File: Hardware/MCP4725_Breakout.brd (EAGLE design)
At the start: 15.2 x 15.2 mm, 17 parts, among them U1 DAC_MCP4725SOT-CP

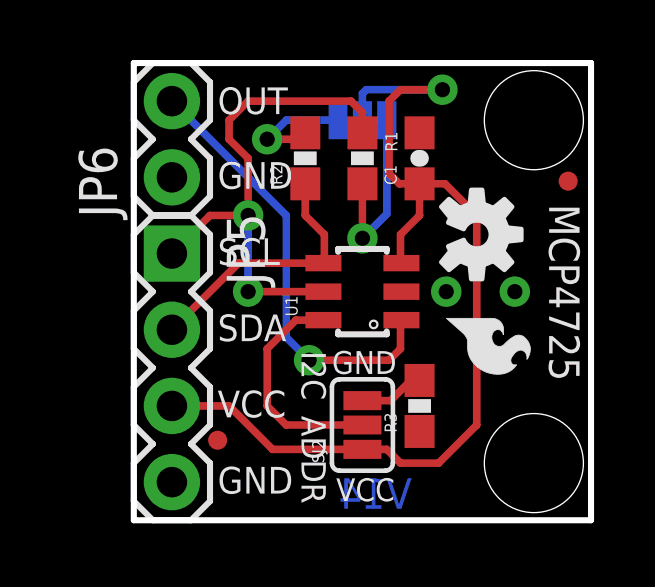
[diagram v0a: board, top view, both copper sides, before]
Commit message: Last Commit before Reds
Added my name to brd. file
added Vcc levels to sch.
changed file name so version # isn't there
minor silk fixes due to vias.
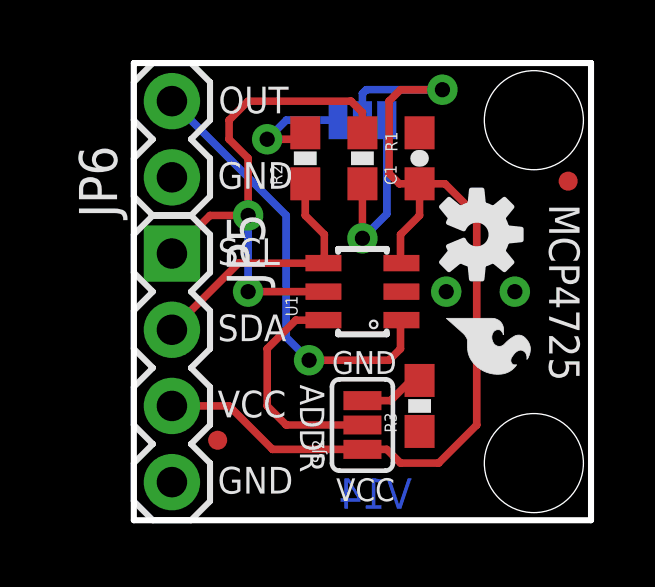
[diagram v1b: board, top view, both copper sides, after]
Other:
- board text added: "Joel Bartlett"
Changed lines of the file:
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@@
 <text x="2.794" y="8.509" size="0.889" layer="21" ratio="15">SCL</text>
 <text x="2.794" y="3.429" size="0.889" layer="21" ratio="15">VCC</text>
-<text x="2.794" y="13.5382" size="0.889" layer="21" ratio="15">OUT</text>
+<text x="2.8194" y="13.5636" size="0.889" layer="21" ratio="15">OUT</text>
 <text x="13.843" y="10.541" size="1.016" layer="21" ratio="15" rot="SR270">MCP4725</text>
 <text x="9.271" y="0.381" size="1.016" layer="16" font="vector" ratio="15" rot="SMR0">V14</text>
-<text x="5.588" y="5.6388" size="0.8128" layer="21" font="vector" ratio="15" rot="SR270">I2C</text>
-<text x="5.588" y="3.4798" size="0.8128" layer="21" font="vector" ratio="15" rot="SR270">ADDR</text>
+<text x="5.5372" y="4.5212" size="0.8128" layer="21" font="vector" ratio="15" rot="SR270">ADDR</text>
 <text x="5.207" y="13.97" size="1.016" layer="22" ratio="15" rot="MR0" align="center-left">OUT</text>
 <text x="5.207" y="8.89" size="1.016" layer="22" ratio="15" rot="MR0" align="center-left">SCL</text>
@@
 <text x="2.794" y="11.049" size="0.889" layer="21" ratio="15">GND</text>
 <text x="5.207" y="11.43" size="1.016" layer="22" ratio="15" rot="MR0" align="center-left">GND</text>
+<text x="52.07" y="-21.59" size="1.778" layer="51">Joel Bartlett</text>
 </plain>
 <attributes>

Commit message: removed micro fiducial, added regulars
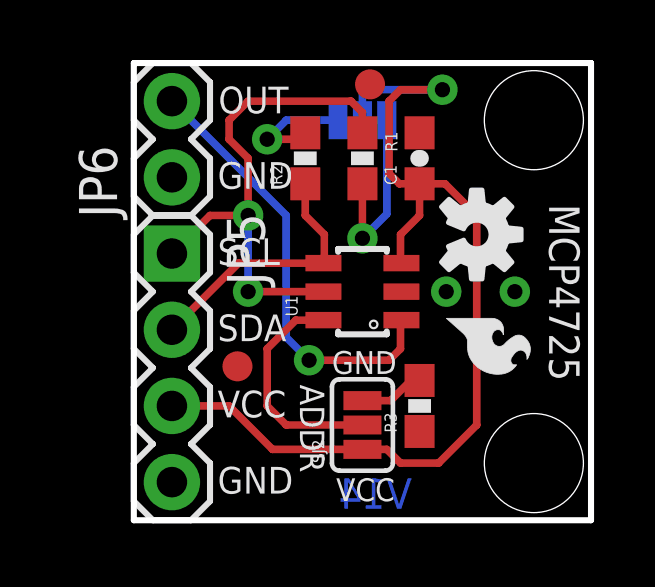
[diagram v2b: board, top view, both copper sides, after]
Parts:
- removed JP2, JP3: FIDUCIALUFIDUCIAL, SparkFun:MICRO-FIDUCIAL
- added FID1, FID2: FIDUCIAL1X2, SparkFun-Aesthetics:FIDUCIAL-1X2

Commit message: changed location of fiducial
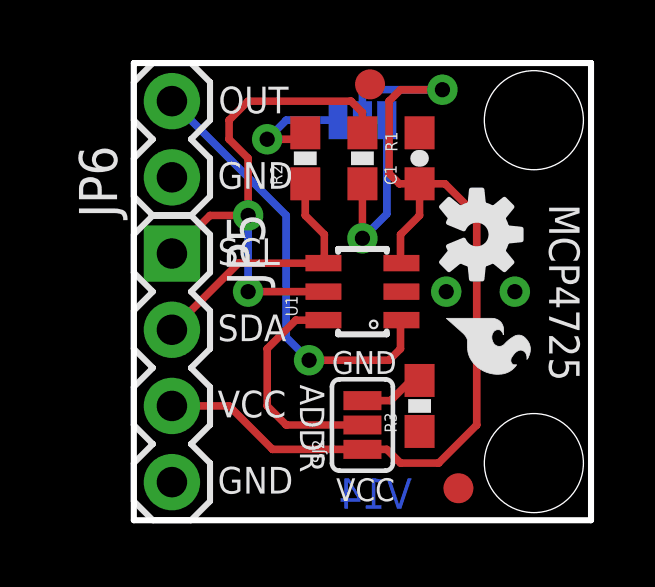
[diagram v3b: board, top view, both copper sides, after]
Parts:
- moved FID1 8.41 mm to (10.8, 1.07)
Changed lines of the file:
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@@
 <setting verticaltext="up"/>
 </settings>
-<grid distance="0.01" unitdist="inch" unit="inch" style="lines" multiple="1" display="yes" altdistance="0.001" altunitdist="inch" altunit="inch"/>
+<grid distance="0.05" unitdist="inch" unit="inch" style="lines" multiple="1" display="yes" altdistance="0.01" altunitdist="inch" altunit="inch"/>
 <layers>
 <layer number="1" name="Top" color="4" fill="1" visible="yes" active="yes"/>
@@
 <element name="SJ2" library="SparkFun-Passives" package="PAD-JUMPER-3-2OF3_NC_BY_PASTE_YES_SILK_FULL_BOX" value="" x="7.62" y="3.175" rot="R90"/>
 <element name="R3" library="SparkFun" package="0603-RES" value="10k" x="9.525" y="3.81" rot="R90"/>
-<element name="FID1" library="SparkFun-Aesthetics" package="FIDUCIAL-1X2" value="FIDUCIAL1X2" x="3.4544" y="5.1308"/>
+<element name="FID1" library="SparkFun-Aesthetics" package="FIDUCIAL-1X2" value="FIDUCIAL1X2" x="10.8204" y="1.0668"/>
 <element name="FID2" library="SparkFun-Aesthetics" package="FIDUCIAL-1X2" value="FIDUCIAL1X2" x="7.874" y="14.5288"/>
 </elements>

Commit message: Corrected to generic SOT-23 library
See engineering file audit, package issues for more information.
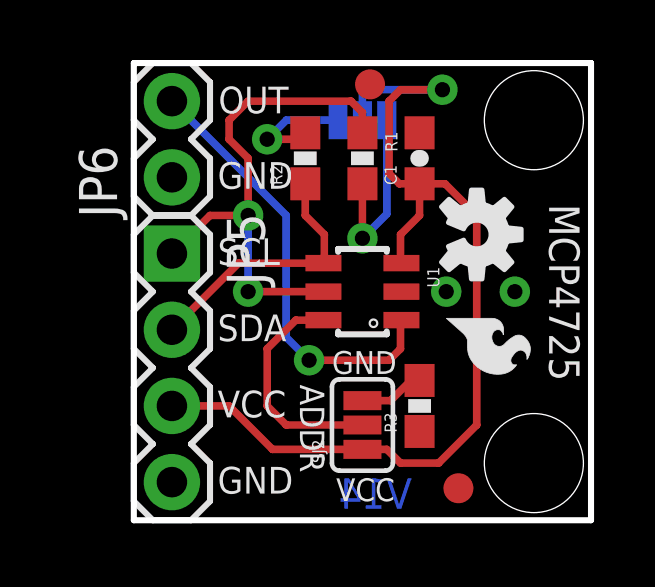
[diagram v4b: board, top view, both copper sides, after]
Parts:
- FRAME2: value FRAME-LETTER -> (none)
- SJ2: value (none) -> JUMPER-PAD-3-2OF3_NC_BY_PASTE
- U1: value DAC_MCP4725SOT-CP -> MCP4725; device SparkFun-AnalogIC:SOT23-6-MCP4725 -> SparkFun-AnalogIC:SOT23-6
- turned U1 to 270 degrees
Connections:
- net N$3: now also U1.6; no longer U1.4
- net SDA: now also U1.4; no longer U1.6
- net VCC: now also U1.3; no longer U1.1
- net VOUT: now also U1.1; no longer U1.3
